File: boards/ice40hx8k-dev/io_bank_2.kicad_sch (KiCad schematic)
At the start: 22 parts, among them U1 ICE40HX8K-CT256

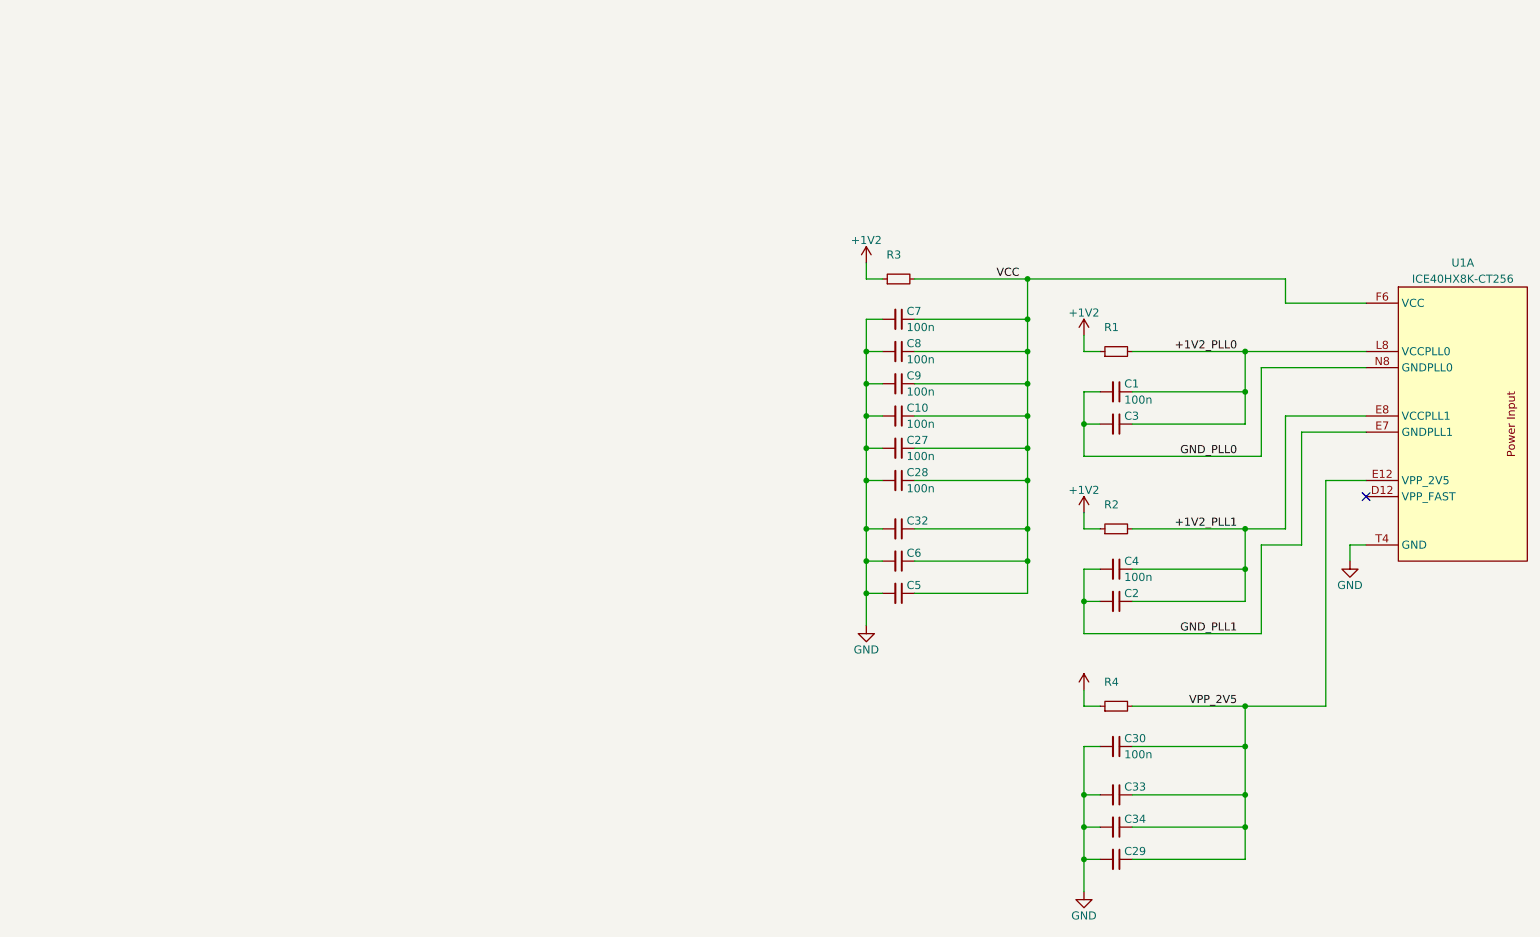
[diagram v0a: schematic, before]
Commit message: Split up schematic and label all nets.
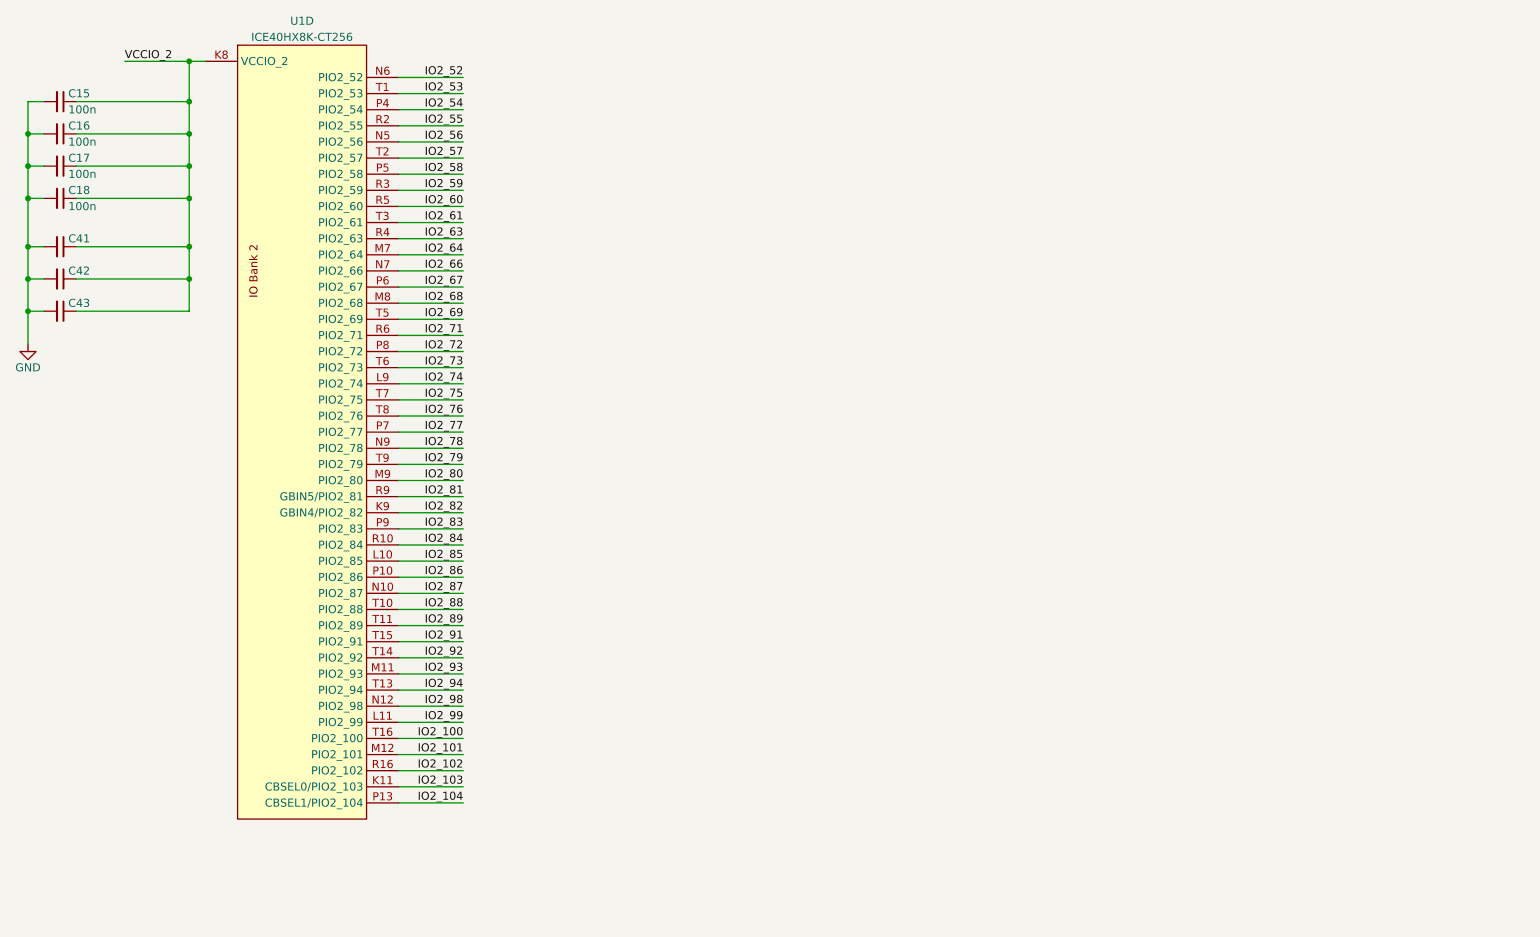
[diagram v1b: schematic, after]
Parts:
- removed C1, C10, C27, C28, C30, C4, C7, C8, C9: 100n, 0Local:C_SMD_0402_Pad0.5mm, symbol Device:C_Small
- removed C2, C29, C3, C32, C33, C34, C5, C6: (no value), 0Local:C_SMD_0402_Pad0.5mm, symbol Device:C_Small
- removed R1, R3: (no value), 0Local:R_SMD_0402_Pad0.5mm, symbol Device:R_Small
- removed R2, R4: (no value), symbol Device:R_Small
- removed U1: ICE40HX8K-CT256, 0Local:Lattice_caBGA-256_14x14mm_Layout16x16_P0.8mm_Ball0.4mm_Pad0.5mm_SMD, symbol 0Local:ICE40HX8K-CT256
- added C15, C16, C17, C18: 100n, 0Local:C_SMD_0402_Pad0.5mm, symbol Device:C_Small
- added C41, C42, C43: (no value), 0Local:C_SMD_0402_Pad0.5mm, symbol Device:C_Small
- added U1: ICE40HX8K-CT256, 0Local:Lattice_caBGA-256_14x14mm_Layout16x16_P0.8mm_Ball0.4mm_Pad0.5mm_SMD, symbol 0Local:ICE40HX8K-CT256
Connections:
- net GND: now also C15.2, C16.2, C17.2, C18.2, C41.2, C42.2, C43.2
- new net IO2_100: U1.T16 (PIO2_100)
- new net IO2_101: U1.M12 (PIO2_101)
- new net IO2_102: U1.R16 (PIO2_102)
- new net IO2_103: U1.K11 (CBSEL0/PIO2_103)
- new net IO2_104: U1.P13 (CBSEL1/PIO2_104)
- new net IO2_52: U1.N6 (PIO2_52)
- new net IO2_53: U1.T1 (PIO2_53)
- new net IO2_54: U1.P4 (PIO2_54)
- new net IO2_55: U1.R2 (PIO2_55)
- new net IO2_56: U1.N5 (PIO2_56)
- new net IO2_57: U1.T2 (PIO2_57)
- new net IO2_58: U1.P5 (PIO2_58)
- new net IO2_59: U1.R3 (PIO2_59)
- new net IO2_60: U1.R5 (PIO2_60)
- new net IO2_61: U1.T3 (PIO2_61)
- new net IO2_63: U1.R4 (PIO2_63)
- new net IO2_64: U1.M7 (PIO2_64)
- new net IO2_66: U1.N7 (PIO2_66)
- new net IO2_67: U1.P6 (PIO2_67)
- new net IO2_68: U1.M8 (PIO2_68)
- new net IO2_69: U1.T5 (PIO2_69)
- new net IO2_71: U1.R6 (PIO2_71)
- new net IO2_72: U1.P8 (PIO2_72)
- new net IO2_73: U1.T6 (PIO2_73)
- new net IO2_74: U1.L9 (PIO2_74)
- new net IO2_75: U1.T7 (PIO2_75)
- new net IO2_76: U1.T8 (PIO2_76)
- new net IO2_77: U1.P7 (PIO2_77)
- new net IO2_78: U1.N9 (PIO2_78)
- new net IO2_79: U1.T9 (PIO2_79)
- new net IO2_80: U1.M9 (PIO2_80)
- new net IO2_81: U1.R9 (GBIN5/PIO2_81)
- new net IO2_82: U1.K9 (GBIN4/PIO2_82)
- new net IO2_83: U1.P9 (PIO2_83)
- new net IO2_84: U1.R10 (PIO2_84)
- new net IO2_85: U1.L10 (PIO2_85)
- new net IO2_86: U1.P10 (PIO2_86)
- new net IO2_87: U1.N10 (PIO2_87)
- new net IO2_88: U1.T10 (PIO2_88)
- new net IO2_89: U1.T11 (PIO2_89)
- new net IO2_91: U1.T15 (PIO2_91)
- new net IO2_92: U1.T14 (PIO2_92)
- new net IO2_93: U1.M11 (PIO2_93)
- new net IO2_94: U1.T13 (PIO2_94)
- new net IO2_98: U1.N12 (PIO2_98)
- new net IO2_99: U1.L11 (PIO2_99)
- new net VCCIO_2: C15.1, C16.1, C17.1, C18.1, C41.1, C42.1, C43.1, U1.K8 (VCCIO_2), U1.P3 (VCCIO_2), U1.R13 (VCCIO_2), U1.R8 (VCCIO_2)
- no-connect marks 1 -> 0

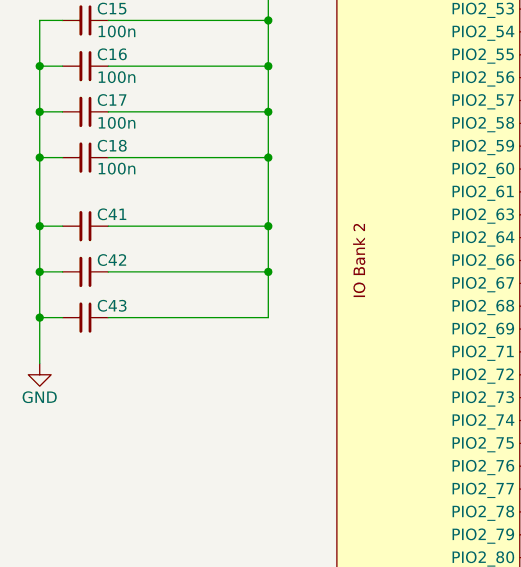
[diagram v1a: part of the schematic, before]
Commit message: Switch to 6 layers, add power fills under BGA.
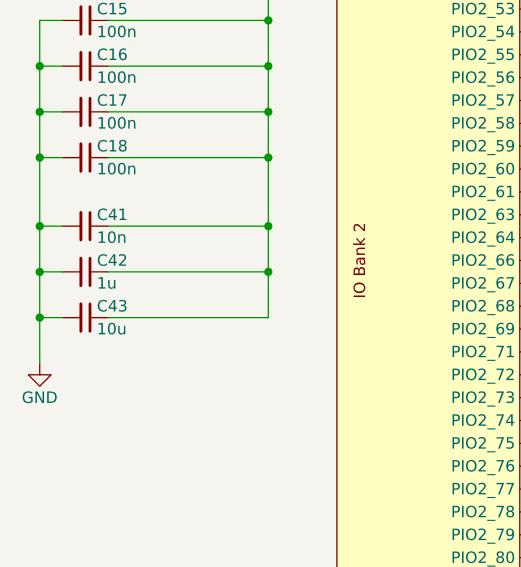
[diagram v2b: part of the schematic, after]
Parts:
- C41: value (none) -> 10n
- C42: value (none) -> 1u
- C43: value (none) -> 10u
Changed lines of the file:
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@@
       (effects (font (size 1.27 1.27)) (justify left))
     )
-    (property "Value" "" (id 1) (at 24.13 68.58 90)
+    (property "Value" "10u" (id 1) (at 24.13 68.58 90)
       (effects (font (size 1.27 1.27)) (justify left))
     )
@@
       (effects (font (size 1.27 1.27)) (justify left))
     )
-    (property "Value" "" (id 1) (at 24.13 63.5 90)
+    (property "Value" "1u" (id 1) (at 24.13 63.5 90)
       (effects (font (size 1.27 1.27)) (justify left))
     )
@@
       (effects (font (size 1.27 1.27)) (justify left))
     )
-    (property "Value" "" (id 1) (at 24.13 58.42 90)
-      (effects (font (size 1.27 1.27)) (justify left))
-    )
+    (property "Value" "10n" (id 1) (at 24.13 58.42 90)
+      (effects (font (size 1.27 1.27)) (justify left))
+    )

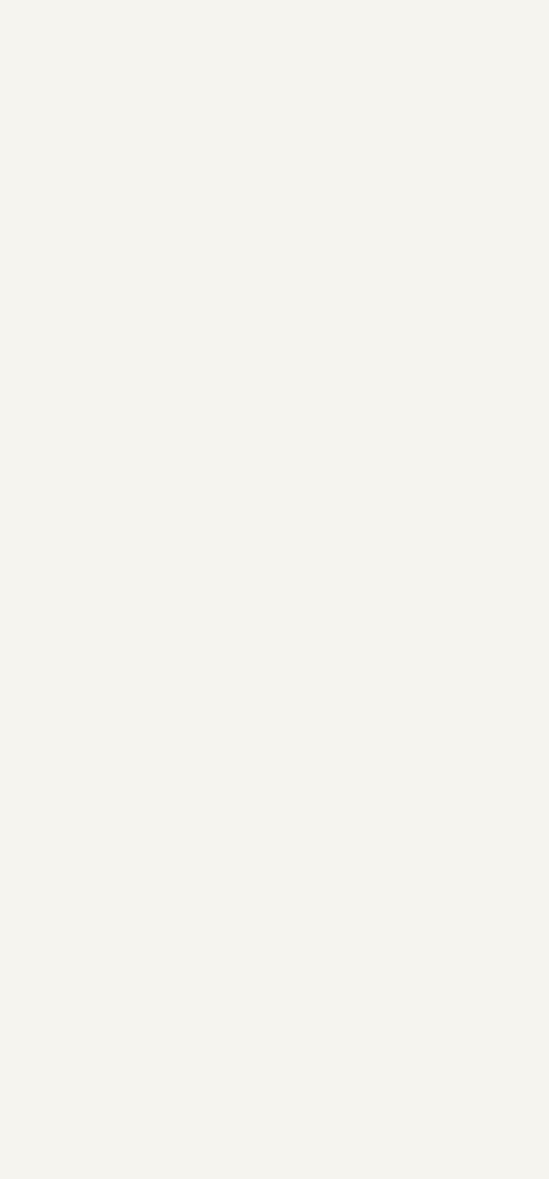
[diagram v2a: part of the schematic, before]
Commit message: Add USB connector and FT2323 symbol.
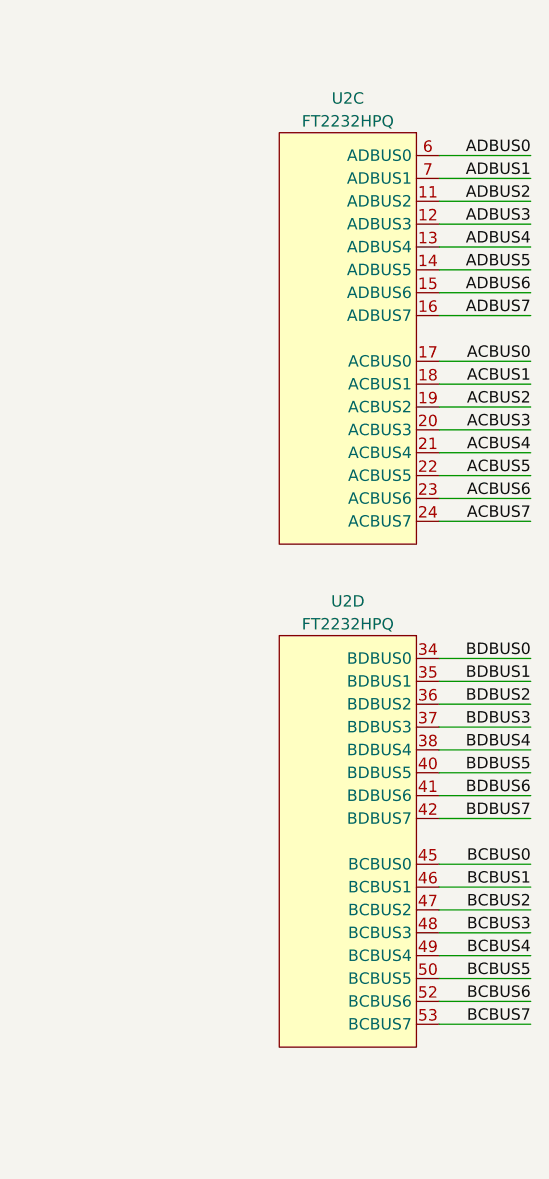
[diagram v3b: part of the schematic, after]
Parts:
- added U2: FT2232HPQ, Package_DFN_QFN:QFN-68-1EP_8x8mm_P0.4mm_EP5.2x5.2mm, symbol 0Local:FT2232HPQ
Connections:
- new net ACBUS0: U2.17 (ACBUS0)
- new net ACBUS1: U2.18 (ACBUS1)
- new net ACBUS2: U2.19 (ACBUS2)
- new net ACBUS3: U2.20 (ACBUS3)
- new net ACBUS4: U2.21 (ACBUS4)
- new net ACBUS5: U2.22 (ACBUS5)
- new net ACBUS6: U2.23 (ACBUS6)
- new net ACBUS7: U2.24 (ACBUS7)
- new net ADBUS0: U2.6 (ADBUS0)
- new net ADBUS1: U2.7 (ADBUS1)
- new net ADBUS2: U2.11 (ADBUS2)
- new net ADBUS3: U2.12 (ADBUS3)
- new net ADBUS4: U2.13 (ADBUS4)
- new net ADBUS5: U2.14 (ADBUS5)
- new net ADBUS6: U2.15 (ADBUS6)
- new net ADBUS7: U2.16 (ADBUS7)
- new net BCBUS0: U2.45 (BCBUS0)
- new net BCBUS1: U2.46 (BCBUS1)
- new net BCBUS2: U2.47 (BCBUS2)
- new net BCBUS3: U2.48 (BCBUS3)
- new net BCBUS4: U2.49 (BCBUS4)
- new net BCBUS5: U2.50 (BCBUS5)
- new net BCBUS6: U2.52 (BCBUS6)
- new net BCBUS7: U2.53 (BCBUS7)
- new net BDBUS0: U2.34 (BDBUS0)
- new net BDBUS1: U2.35 (BDBUS1)
- new net BDBUS2: U2.36 (BDBUS2)
- new net BDBUS3: U2.37 (BDBUS3)
- new net BDBUS4: U2.38 (BDBUS4)
- new net BDBUS5: U2.40 (BDBUS5)
- new net BDBUS6: U2.41 (BDBUS6)
- new net BDBUS7: U2.42 (BDBUS7)

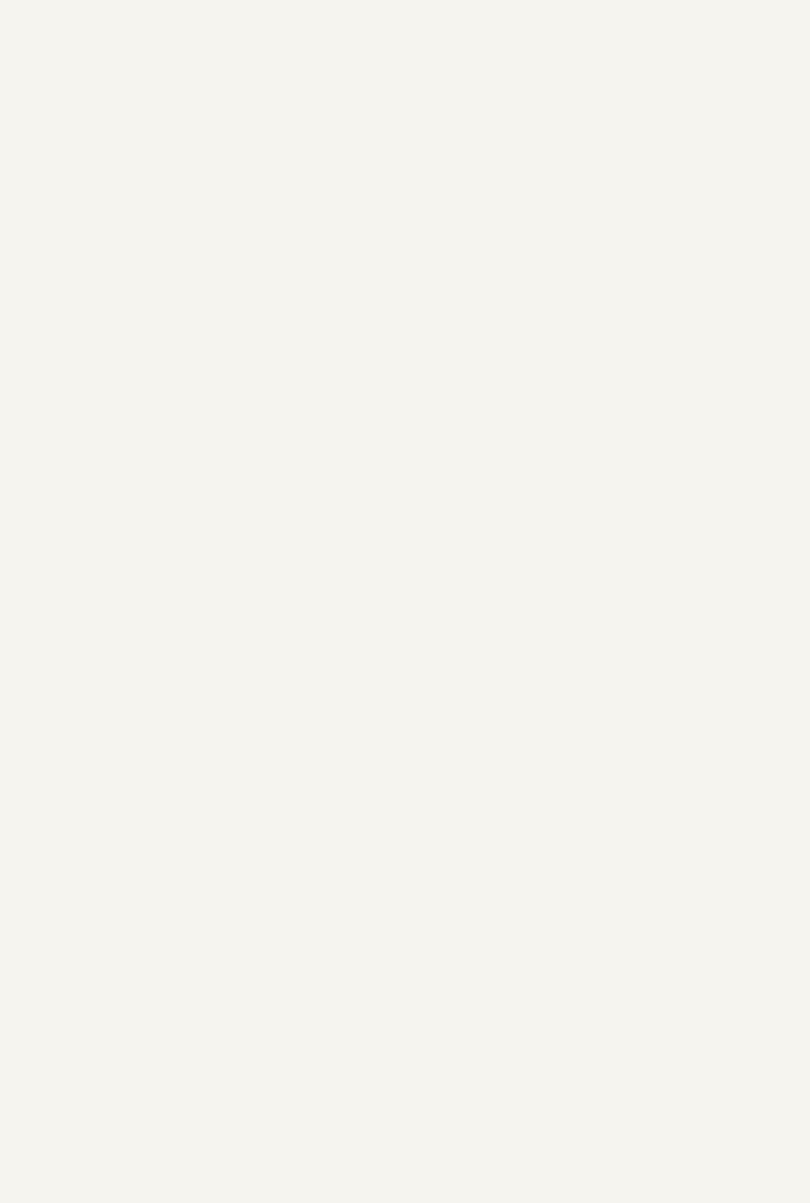
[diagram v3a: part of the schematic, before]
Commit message: Add Hirose connectors and standoffs.
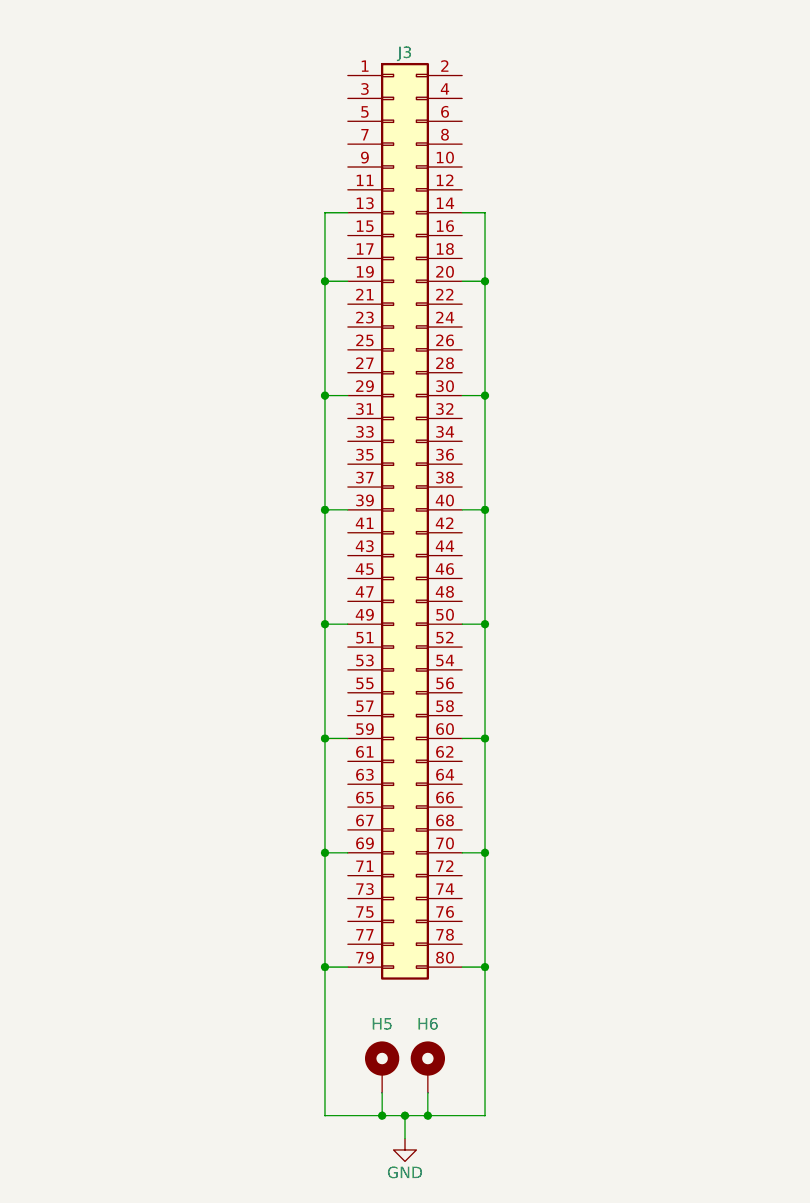
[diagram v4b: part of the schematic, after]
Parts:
- added H5, H6: 9774020633, Mounting_Wuerth:Mounting_Wuerth_WA-SMSI-M1.6_H2mm_9774020633, symbol Mechanical:MountingHole_Pad
- added J3: DF40HC(4.0)-80DS, 0Local:Hirose_DF40C-80DS, symbol Connector_Generic:Conn_02x40_Odd_Even
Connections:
- net GND: now also H5.1, H6.1, J3.13 (Pin_13), J3.14 (Pin_14), J3.19 (Pin_19), J3.20 (Pin_20), J3.29 (Pin_29), J3.30 (Pin_30), J3.39 (Pin_39), J3.40 (Pin_40), J3.49 (Pin_49), J3.50 (Pin_50), J3.59 (Pin_59), J3.60 (Pin_60), J3.69 (Pin_69), J3.70 (Pin_70), J3.79 (Pin_79), J3.80 (Pin_80)

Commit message: Switch to 4mm Hirose connectors and different mounting holes.
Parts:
- H5, H6: footprint Mounting_Wuerth:Mounting_Wuerth_WA-SMSI-M1.6_H2mm_9774020633 -> 0Local:MountingHole_2.2mm_M2_Pad6mm
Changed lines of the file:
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@@
       (effects (font (size 1.27 1.27)) hide)
     )
-    (property "Footprint" "Mounting_Wuerth:Mounting_Wuerth_WA-SMSI-M1.6_H2mm_9774020633" (id 2) (at 149.86 137.16 0)
+    (property "Footprint" "0Local:MountingHole_2.2mm_M2_Pad6mm" (id 2) (at 149.86 137.16 0)
       (effects (font (size 1.27 1.27)) hide)
     )
@@
       (effects (font (size 1.27 1.27)) hide)
     )
-    (property "Footprint" "Mounting_Wuerth:Mounting_Wuerth_WA-SMSI-M1.6_H2mm_9774020633" (id 2) (at 154.94 137.16 0)
+    (property "Footprint" "0Local:MountingHole_2.2mm_M2_Pad6mm" (id 2) (at 154.94 137.16 0)
       (effects (font (size 1.27 1.27)) hide)
     )
